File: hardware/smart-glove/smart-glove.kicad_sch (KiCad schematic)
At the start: 29 parts, among them J1 USB-C, J2 FLEX, J3 LiPo, SW1 BOOT, SW2 EN, U1 ESP32-WROOM-32E, U2 TP4056, U3 AMS1117-3.3, U4 MPU-6050

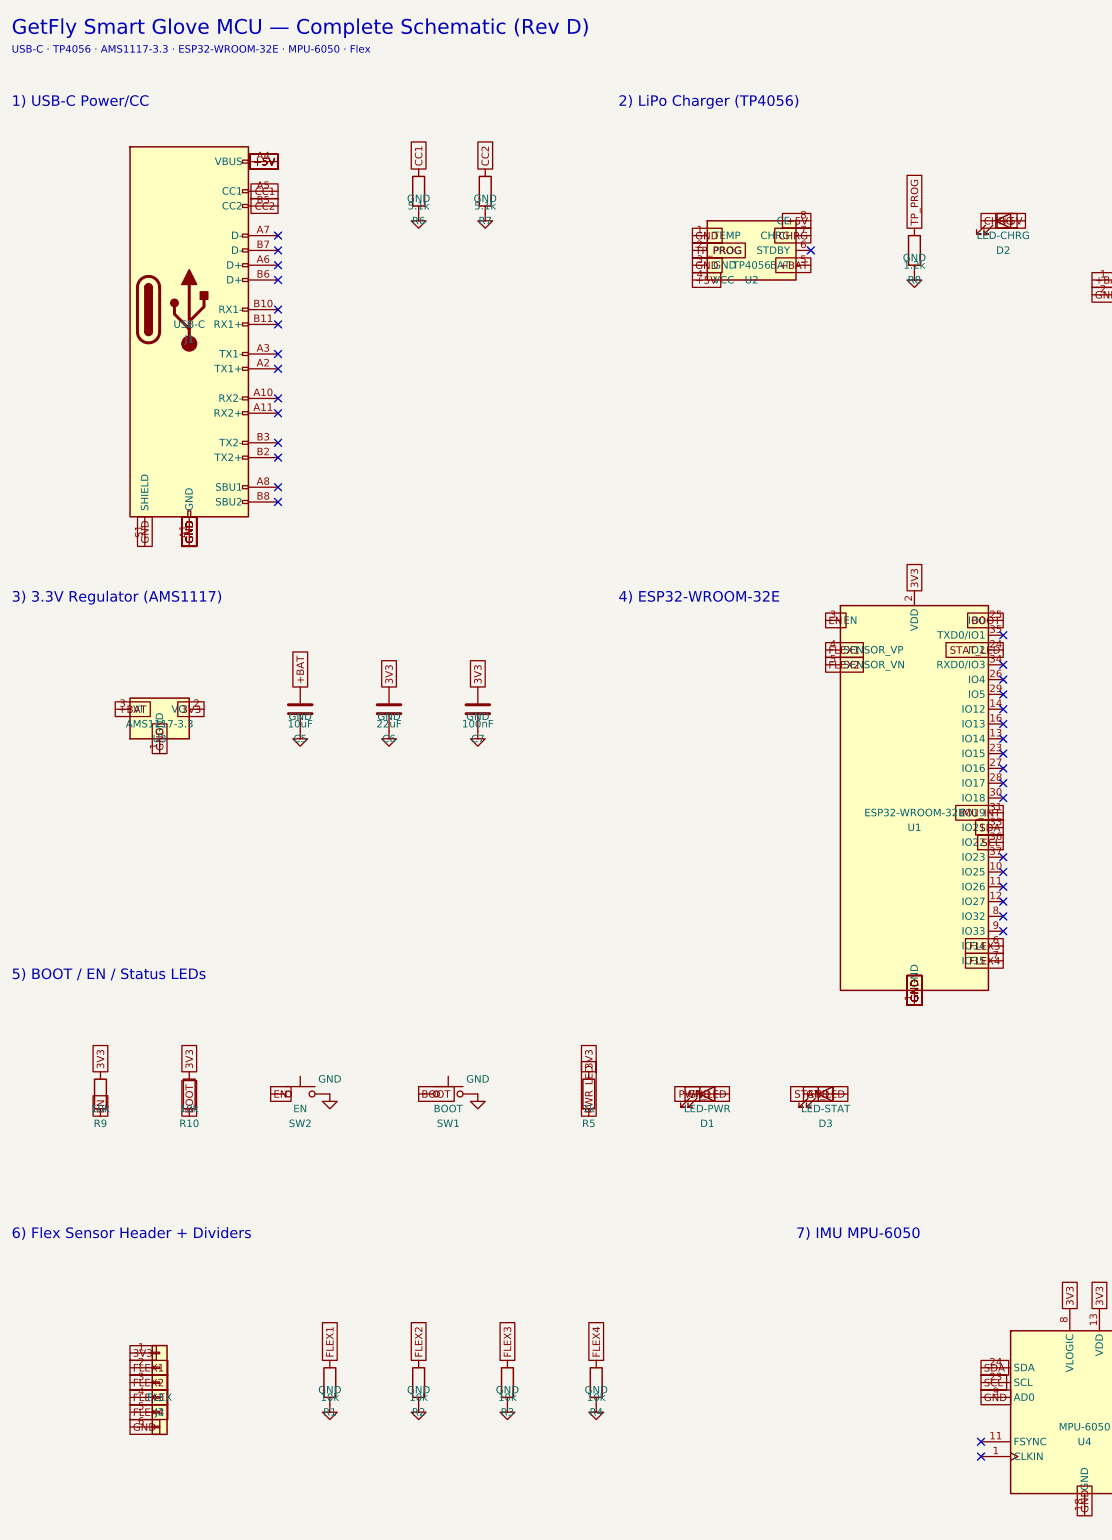
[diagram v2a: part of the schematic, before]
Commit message: Rev E: 5 flex sensors + SignSpeak / Man Who Embed branding
J2 is 1x7 (3V3 + FLEX1-5 + GND), R11 divider, ESP32 GPIO32=FLEX5.
Schematic ERC 0 errors; silkscreen and docs renamed for SignSpeak.

Co-authored-by: ADIL ZAHOOR  <adilzahoor2812@users.noreply.github.com>
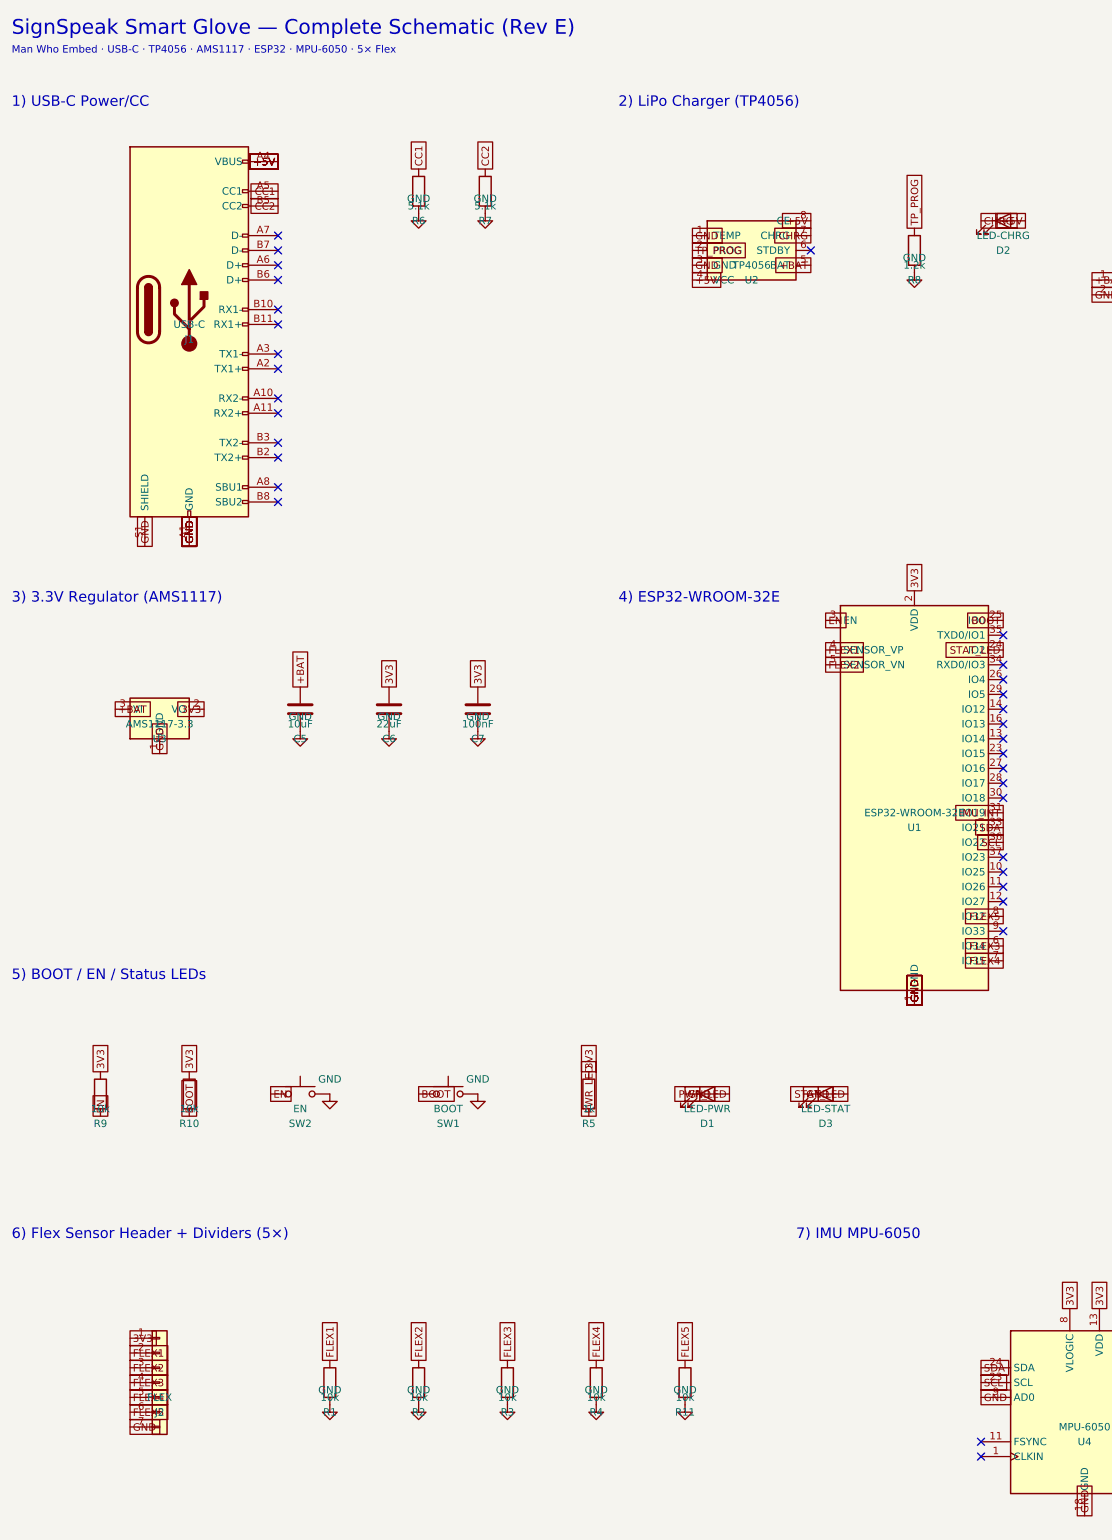
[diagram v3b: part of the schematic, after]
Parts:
- removed J2: FLEX, Connector_PinHeader_2.54mm:PinHeader_1x06_P2.54mm_Vertical, symbol Connector_Generic:Conn_01x06
- added J2: FLEX, Connector_PinHeader_2.54mm:PinHeader_1x07_P2.54mm_Vertical, symbol Connector_Generic:Conn_01x07
- added R11: 10k, Resistor_SMD:R_0603_1608Metric, symbol Device:R
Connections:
- net 3V3: now also J2.1 (Pin_1)
- net FLEX1: now also J2.2 (Pin_2)
- net FLEX2: now also J2.3 (Pin_3)
- net FLEX3: now also J2.4 (Pin_4)
- net FLEX4: now also J2.5 (Pin_5)
- net GND: now also J2.7 (Pin_7), R11.2
- net FLEX5: now reaches U1.8 (IO32)
- net FLEX5: now also J2.6 (Pin_6), R11.1
- no-connect marks 37 -> 36
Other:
- note added: "6) Flex Sensor Header + Dividers (5×)"
- note added: "Man Who Embed · USB-C · TP4056 · AMS1117 · ESP32 · MPU-6050 · 5× Flex"
- note added: "SignSpeak Smart Glove — Complete Schematic (Rev E)"
- note removed: "6) Flex Sensor Header + Dividers"
- note removed: "GetFly Smart Glove MCU — Complete Schematic (Rev D)"
- note removed: "USB-C · TP4056 · AMS1117-3.3 · ESP32-WROOM-32E · MPU-6050 · Flex"
- company: GetFly -> Man Who Embed
- title: GetFly Smart Glove MCU -> SignSpeak Smart Glove
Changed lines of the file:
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@@
   (paper "A2")
   (title_block
-    (title "GetFly Smart Glove MCU")
+    (title "SignSpeak Smart Glove")
     (date "2026-07-18")
-    (rev "D")
-    (company "GetFly")
-    (comment 1 "Complete schematic: ESP32 / TP4056 / AMS1117 / MPU-6050 / Flex / USB-C")
-  )
-  (text "GetFly Smart Glove MCU — Complete Schematic (Rev D)" (exclude_from_sim no) (at 25.4 12.7 0) (effects (font (size 2.54 2.54)) (justify left))
-  )
-  (text "USB-C · TP4056 · AMS1117-3.3 · ESP32-WROOM-32E · MPU-6050 · Flex" (exclude_from_sim no) (at 25.4 16.51 0) (effects (font (size 1.27 1.27)) (justify left))
+    (rev "E")
+    (company "Man Who Embed")
+    (comment 1 "5× flex · ESP32 · TP4056 · AMS1117 · MPU-6050 · USB-C")
+  )
+  (text "SignSpeak Smart Glove — Complete Schematic (Rev E)" (exclude_from_sim no) (at 25.4 12.7 0) (effects (font (size 2.54 2.54)) (justify left))
+  )
+  (text "Man Who Embed · USB-C · TP4056 · AMS1117 · ESP32 · MPU-6050 · 5× Flex" (exclude_from_sim no) (at 25.4 16.51 0) (effects (font (size 1.27 1.27)) (justify left))
   )
   (text "1) USB-C Power/CC" (exclude_from_sim no) (at 25.4 25.4 0) (effects (font (size 1.8 1.8)) (justify left))
@@
   (global_label "FLEX4" (shape passive) (at 195.58 172.72 180) (effects (font (size 1.27 1.27)) (justify right))
   )
+  (global_label "FLEX5" (shape passive) (at 195.58 165.1 180) (effects (font (size 1.27 1.27)) (justify right))
+  )
   (global_label "GND" (shape passive) (at 180.34 180.34 90) (effects (font (size 1.27 1.27)) (justify left))
   )
@@
   (global_label "GND" (shape passive) (at 180.34 180.34 90) (effects (font (size 1.27 1.27)) (justify left))
   )
-  (no_connect (at 195.58 165.1))
   (no_connect (at 195.58 167.64))
   (no_connect (at 195.58 157.48))
@@
   (global_label "STAT_LED" (shape passive) (at 168.91 195.58 180) (effects (font (size 1.27 1.27)) (justify right))
   )
-  (text "6) Flex Sensor Header + Dividers" (exclude_from_sim no) (at 25.4 219.71 0) (effects (font (size 1.8 1.8)) (justify left))
-  )
-  (symbol (lib_id "Connector_Generic:Conn_01x06") (at 50.8 245.11 0) (unit 1) (in_bom yes) (on_board yes) (dnp no)
+  (text "6) Flex Sensor Header + Dividers (5×)" (exclude_from_sim no) (at 25.4 219.71 0) (effects (font (size 1.8 1.8)) (justify left))
+  )
+  (symbol (lib_id "Connector_Generic:Conn_01x07") (at 50.8 245.11 0) (unit 1) (in_bom yes) (on_board yes) (dnp no)
     (property "Reference" "J2" (at 50.8 250.19 0) (effects (font (size 1.27 1.27))))
     (property "Value" "FLEX" (at 50.8 247.65 0) (effects (font (size 1.27 1.27))))
-    (property "Footprint" "Connector_PinHeader_2.54mm:PinHeader_1x06_P2.54mm_Vertical" (at 50.8 245.11 0) (effects (font (size 1.27 1.27)) hide))
+    (property "Footprint" "Connector_PinHeader_2.54mm:PinHeader_1x07_P2.54mm_Vertical" (at 50.8 245.11 0) (effects (font (size 1.27 1.27)) hide))
     (property "Datasheet" "" (at 50.8 245.11 0) (effects (font (size 1.27 1.27)) hide))
   )
-  (global_label "3V3" (shape passive) (at 45.72 240.03 0) (effects (font (size 1.27 1.27)) (justify left))
-  )
-  (global_label "FLEX1" (shape passive) (at 45.72 242.57 0) (effects (font (size 1.27 1.27)) (justify left))
-  )
-  (global_label "FLEX2" (shape passive) (at 45.72 245.11 0) (effects (font (size 1.27 1.27)) (justify left))
-  )
-  (global_label "FLEX3" (shape passive) (at 45.72 247.65 0) (effects (font (size 1.27 1.27)) (justify left))
-  )
-  (global_label "FLEX4" (shape passive) (at 45.72 250.19 0) (effects (font (size 1.27 1.27)) (justify left))
+  (global_label "3V3" (shape passive) (at 45.72 237.49 0) (effects (font (size 1.27 1.27)) (justify left))
+  )
+  (global_label "FLEX1" (shape passive) (at 45.72 240.03 0) (effects (font (size 1.27 1.27)) (justify left))
+  )
+  (global_label "FLEX2" (shape passive) (at 45.72 242.57 0) (effects (font (size 1.27 1.27)) (justify left))
+  )
+  (global_label "FLEX3" (shape passive) (at 45.72 245.11 0) (effects (font (size 1.27 1.27)) (justify left))
+  )
+  (global_label "FLEX4" (shape passive) (at 45.72 247.65 0) (effects (font (size 1.27 1.27)) (justify left))
+  )
+  (global_label "FLEX5" (shape passive) (at 45.72 250.19 0) (effects (font (size 1.27 1.27)) (justify left))
   )
   (global_label "GND" (shape passive) (at 45.72 252.73 0) (effects (font (size 1.27 1.27)) (justify left))
@@
     (property "Datasheet" "" (at 125.73 248.92 0) (effects (font (size 1.27 1.27)) hide))
   )
+  (symbol (lib_id "Device:R") (at 140.97 245.11 0) (unit 1) (in_bom yes) (on_board yes) (dnp no)
+    (property "Reference" "R11" (at 140.97 250.19 0) (effects (font (size 1.27 1.27))))
+    (property "Value" "10k" (at 140.97 247.65 0) (effects (font (size 1.27 1.27))))
+    (property "Footprint" "Resistor_SMD:R_0603_1608Metric" (at 140.97 245.11 0) (effects (font (size 1.27 1.27)) hide))
+    (property "Datasheet" "" (at 140.97 245.11 0) (effects (font (size 1.27 1.27)) hide))
+  )
+  (global_label "FLEX5" (shape passive) (at 140.97 241.3 90) (effects (font (size 1.27 1.27)) (justify left))
+  )
+  (symbol (lib_id "power:GND") (at 140.97 248.92 0) (unit 1) (in_bom yes) (on_board yes) (dnp no)
+    (property "Reference" "#PWR_R11" (at 140.97 251.46 0) (effects (font (size 1.27 1.27)) hide))
+    (property "Value" "GND" (at 140.97 246.38 0) (effects (font (size 1.27 1.27))))
+    (property "Footprint" "" (at 140.97 248.92 0) (effects (font (size 1.27 1.27)) hide))
+    (property "Datasheet" "" (at 140.97 248.92 0) (effects (font (size 1.27 1.27)) hide))
+  )
   (text "7) IMU MPU-6050" (exclude_from_sim no) (at 160.02 219.71 0) (effects (font (size 1.8 1.8)) (justify left))

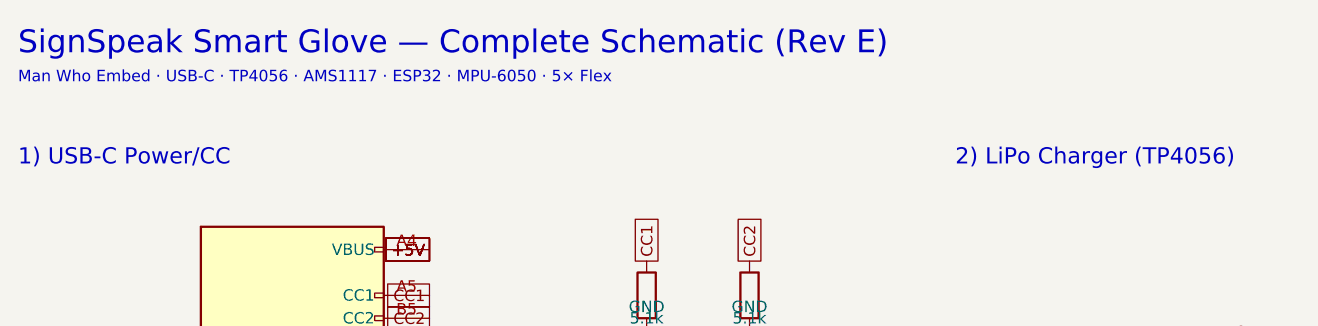
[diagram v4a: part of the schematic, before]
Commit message: Rev F: 75×52 mm SignSpeak glove-back PCB, DRC gate PASS
Shrink from 95×72 to a dorsal-glove outline with horizontal 1×7 flex
header, cleared H4/J3 hole clearance, and refreshed Gerbers/BOM/CPL.

Co-authored-by: ADIL ZAHOOR  <adilzahoor2812@users.noreply.github.com>
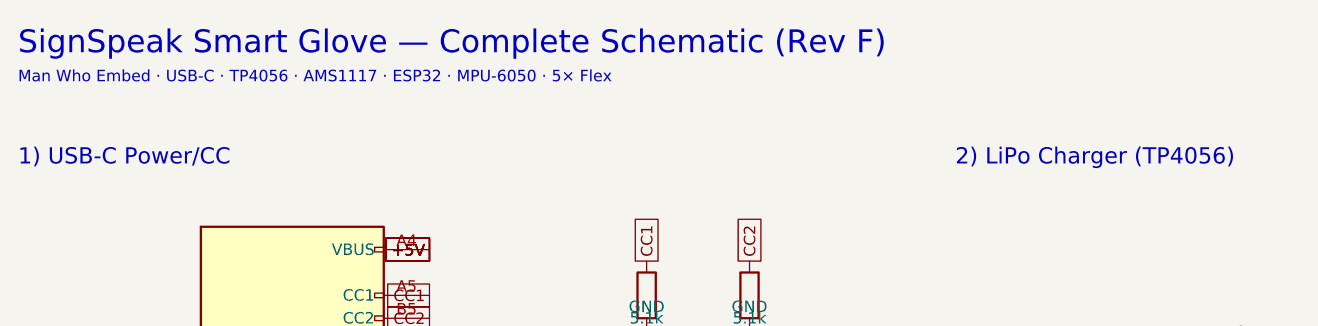
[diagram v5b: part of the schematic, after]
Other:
- note added: "SignSpeak Smart Glove — Complete Schematic (Rev F)"
- note removed: "SignSpeak Smart Glove — Complete Schematic (Rev E)"
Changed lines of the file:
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@@
     (title "SignSpeak Smart Glove")
     (date "2026-07-18")
-    (rev "E")
+    (rev "F")
     (company "Man Who Embed")
     (comment 1 "5× flex · ESP32 · TP4056 · AMS1117 · MPU-6050 · USB-C")
   )
-  (text "SignSpeak Smart Glove — Complete Schematic (Rev E)" (exclude_from_sim no) (at 25.4 12.7 0) (effects (font (size 2.54 2.54)) (justify left))
+  (text "SignSpeak Smart Glove — Complete Schematic (Rev F)" (exclude_from_sim no) (at 25.4 12.7 0) (effects (font (size 2.54 2.54)) (justify left))
   )
   (text "Man Who Embed · USB-C · TP4056 · AMS1117 · ESP32 · MPU-6050 · 5× Flex" (exclude_from_sim no) (at 25.4 16.51 0) (effects (font (size 1.27 1.27)) (justify left))
